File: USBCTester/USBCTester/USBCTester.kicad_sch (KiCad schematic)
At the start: 79 parts, among them J1 USB4080-03-A, J2 USB4080-03-A, J3 Conn_01x14, J4 Conn_01x03, J6 Conn_01x03, SW1 SW_Push, U1 74HC595, U2 74HC595, U3 74HC595, U4 74HC595, U5 74HC595, U6 74HC595, U7 RaspberryPi_Pico

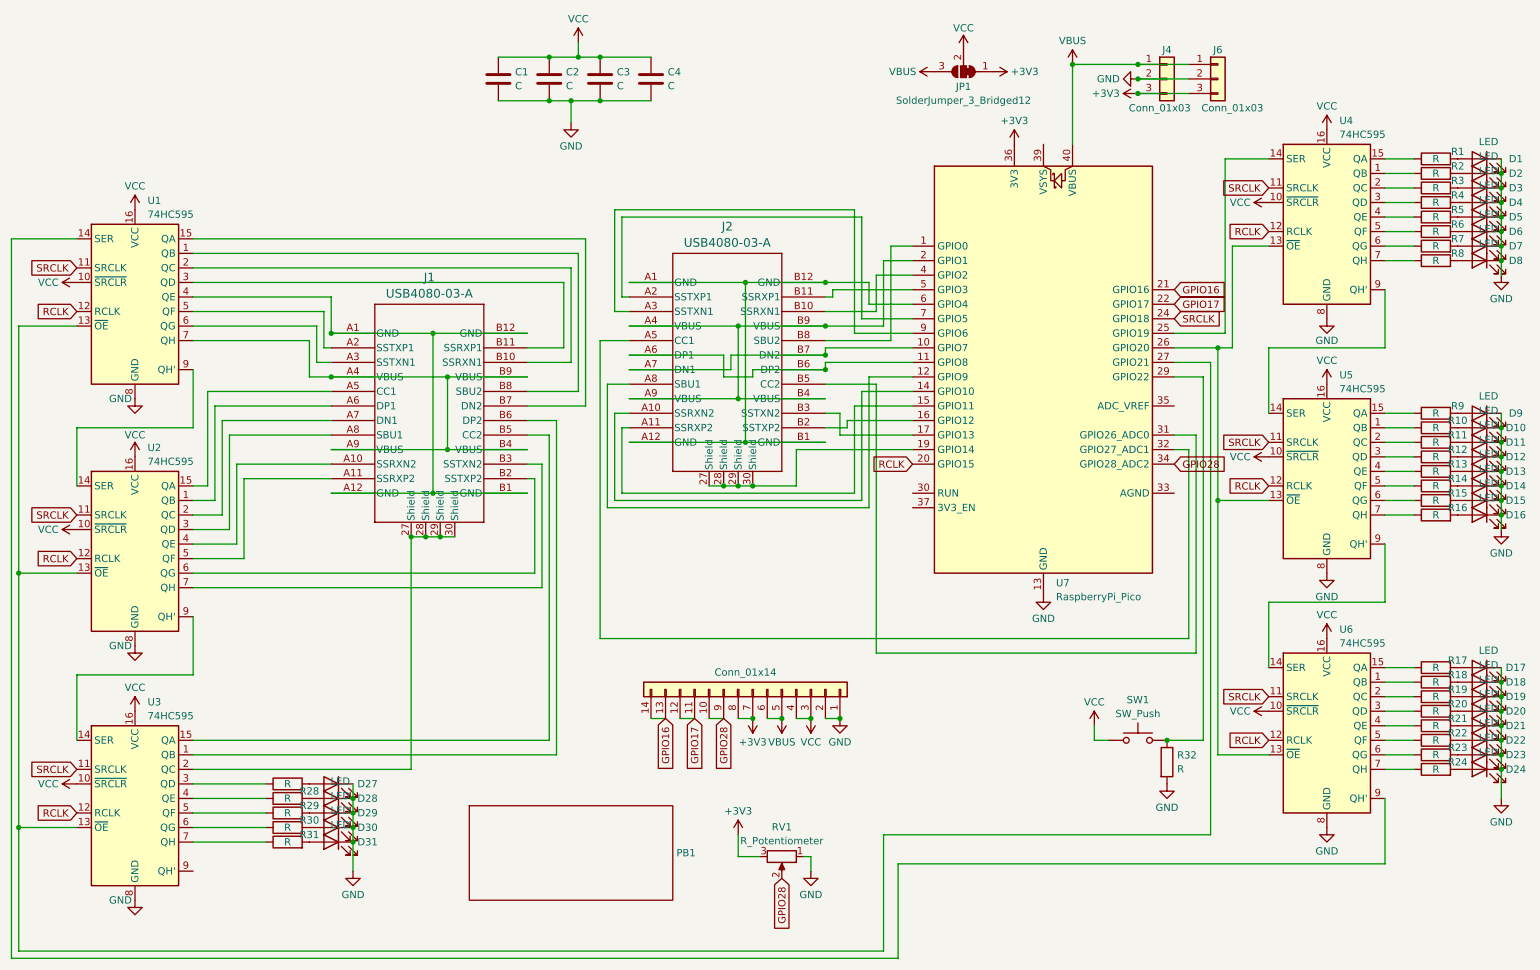
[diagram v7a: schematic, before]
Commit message: many tweaks to finalize design, then Schematic update for safety with external devices
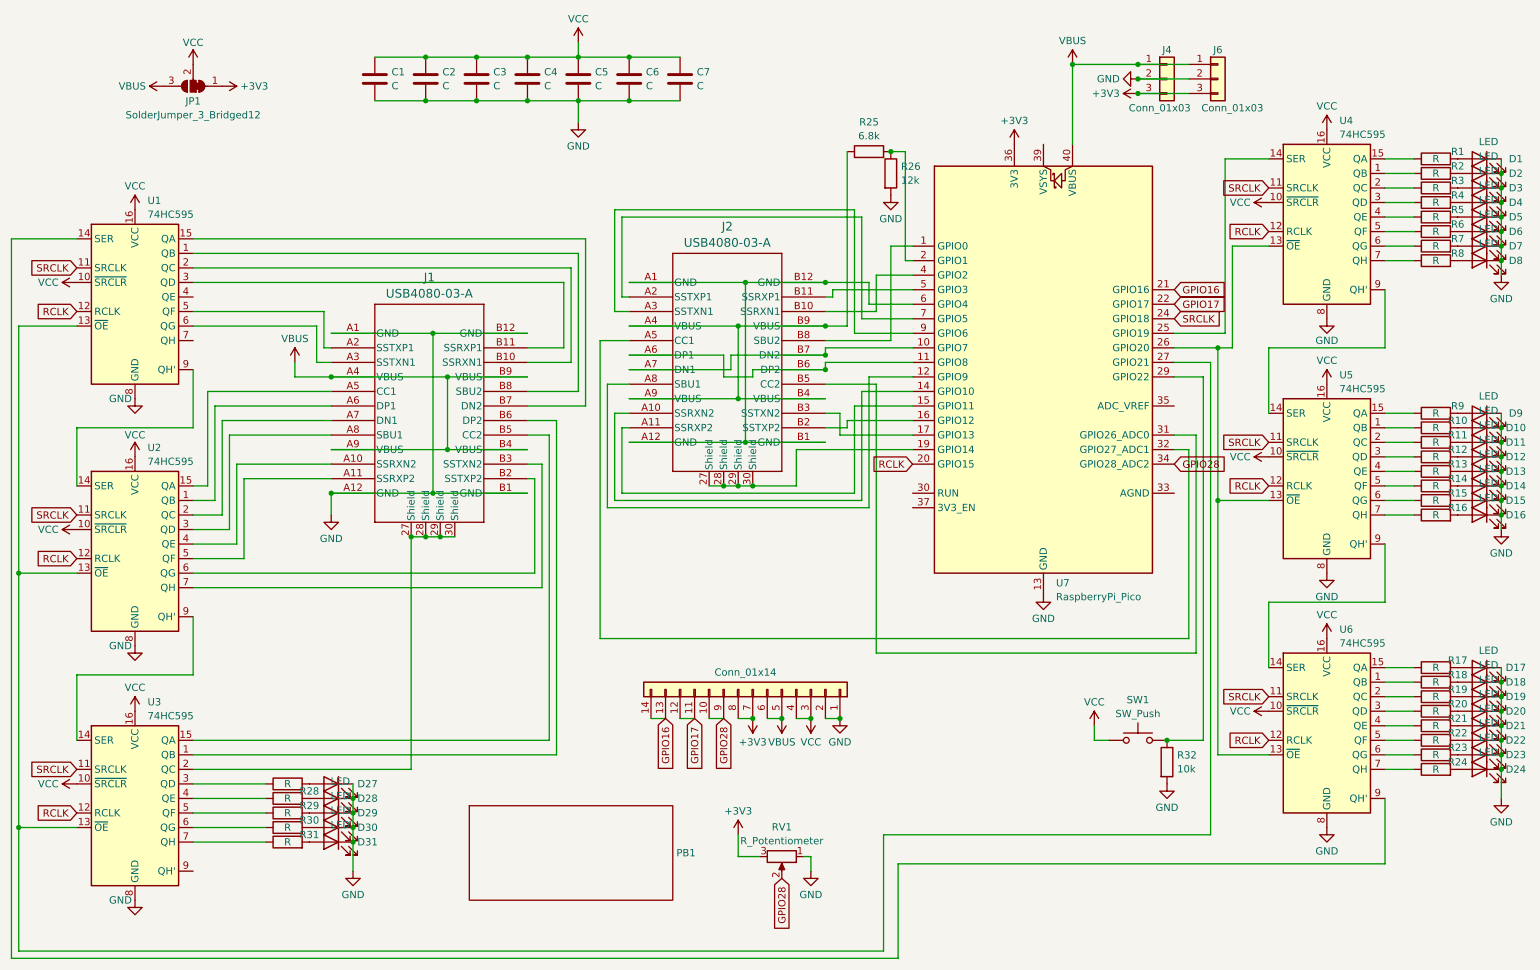
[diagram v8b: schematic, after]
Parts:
- added C5, C6, C7: C, Capacitor_SMD:C_0603_1608Metric, symbol Device:C
- added R25: 6.8k, symbol Device:R
- added R26: 12k, symbol Device:R
- R32: value R -> 10k
- RV1: footprint Potentiometer_SMD:Potentiometer_Vishay_TS53YL_Vertical -> Potentiometer_SMD:TRIM_35WR10KLFTR
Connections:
- net GND: now also J1.A1 (GND), J1.A12 (GND), J1.B1 (GND), J1.B12 (GND), C5.2, C6.2, C7.2, R26.2
- net VBUS: now also J1.A4 (VBUS), J1.A9 (VBUS), J1.B4 (VBUS), J1.B9 (VBUS)
- net VCC: now also C5.1, C6.1, C7.1
- net at J2.A4 (VBUS), J2.A9 (VBUS), J2.B4 (VBUS)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: now also R25.1; no longer U7.2 (GPIO1)
- new net: R25.2, R26.1, U7.2 (GPIO1)
- now unconnected: U1.4 (QE), U1.7 (QH)
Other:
- moved on the sheet: C1, C2, C3, C4, JP1
